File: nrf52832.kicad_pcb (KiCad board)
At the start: 2 copper layers, 66 parts, among them SW1 SW_Push, U1 nRF52832-QFxx, U2 AMS1117-3.3, U3 SX1308, U4 TP4056, U5 MC34063AD, U6 HT7127-1-SOT89, U7 TagConnect, Y1 32MHz

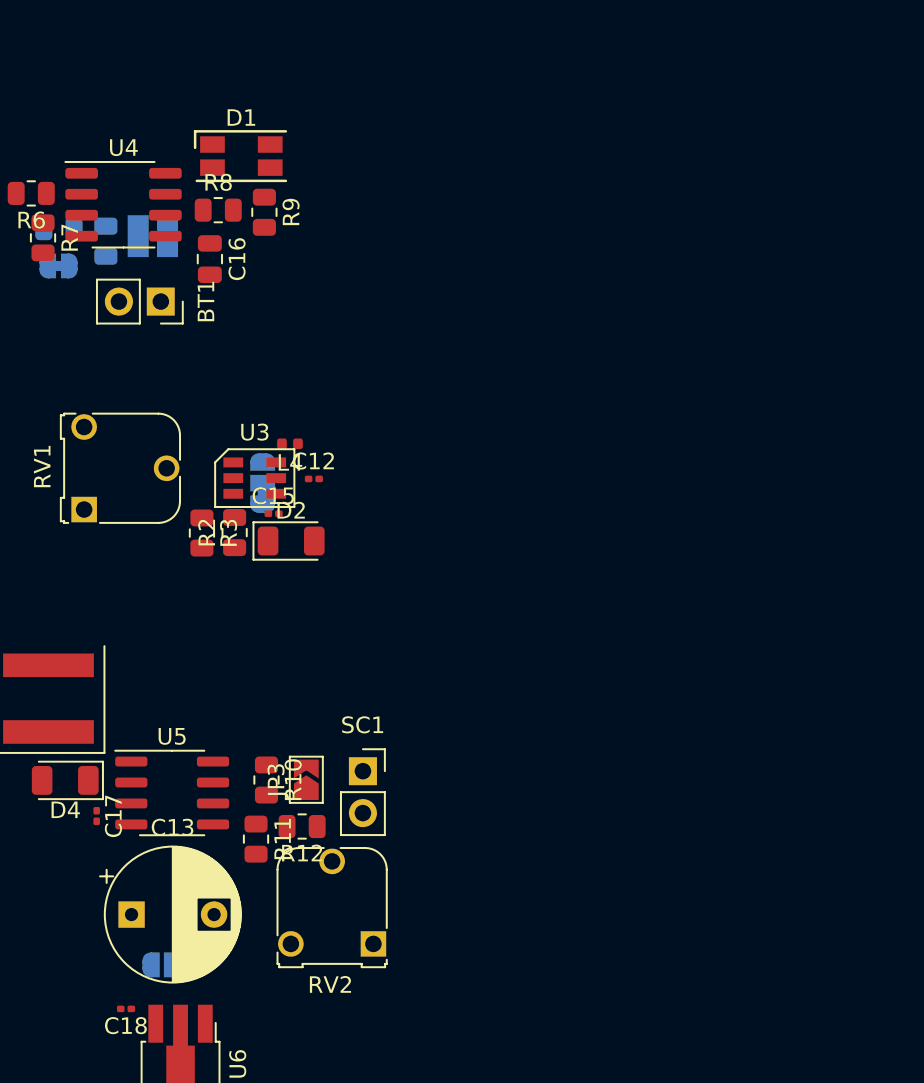
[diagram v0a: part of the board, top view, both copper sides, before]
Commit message: added AC power
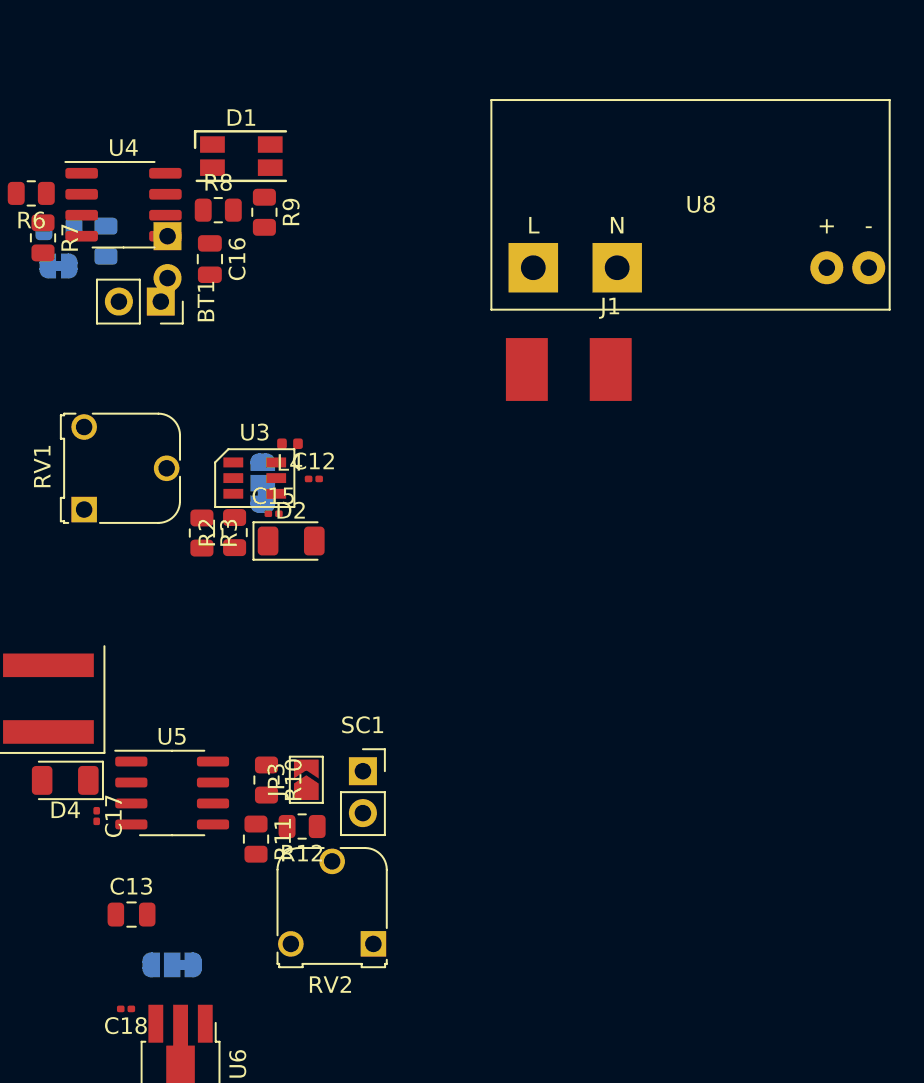
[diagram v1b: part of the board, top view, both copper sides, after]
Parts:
- added J1: Conn_01x02, smdpad:smdpad_01x02_2.54_3.81_2.54, F.Cu at (187.9, 56.0)
- added U8: WX-DC12003, aliexpress:WX-DC12003_vertical, F.Cu at (190.8, 44.8)
- C13: footprint Capacitor_THT:CP_Radial_D8.0mm_P5.00mm -> Capacitor_SMD:C_0805_2012Metric
- TH1: footprint smdpad:smdpad_01x02_1.27_2.54_0.51 -> Connector_PinSocket_2.54mm:PinSocket_1x02_P2.54mm_Vertical
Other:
- net class AC added: clearance 0.5, trace_width 1, via_dia 0.8, via_drill 0.5

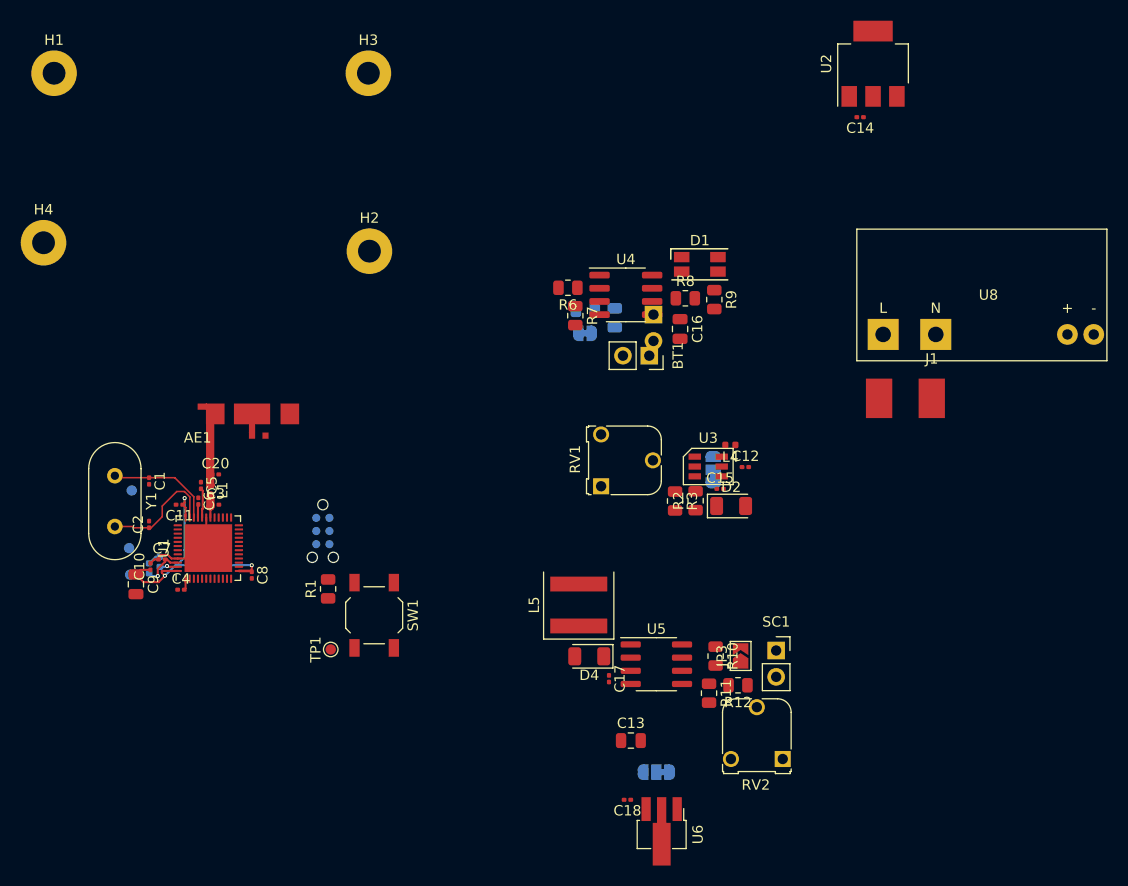
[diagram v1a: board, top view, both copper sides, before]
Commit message: optimized silkscreen
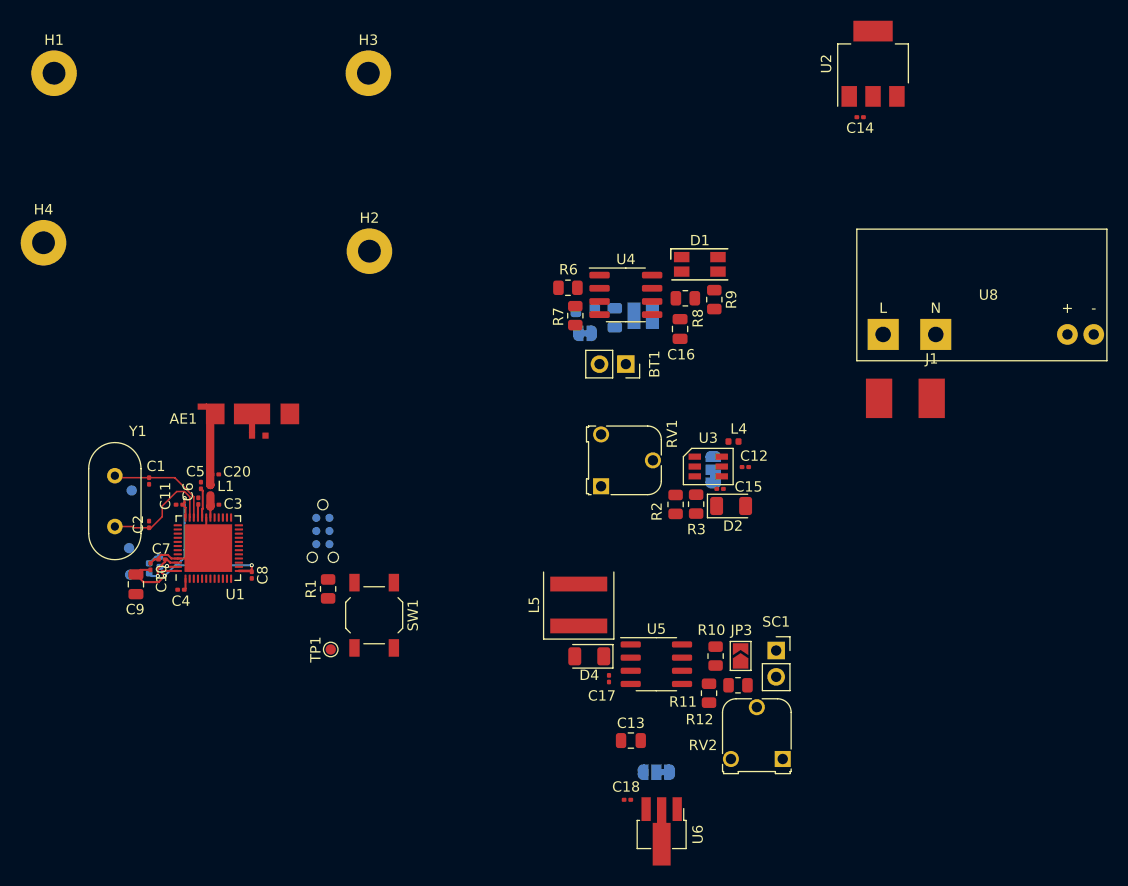
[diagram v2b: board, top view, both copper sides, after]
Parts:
- TH1: footprint Connector_PinSocket_2.54mm:PinSocket_1x02_P2.54mm_Vertical -> smdpad:smdpad_01x02_1.27_2.54_0.51
- moved BT1 2.40 mm to (158.4, 52.7)
- moved L4 0.45 mm to (168.8, 60.2)
- moved R3 0.33 mm to (163.2, 66.3)
- moved R2 0.33 mm to (165.2, 66.2)
- moved TH1 0.14 mm to (161.0, 48.1)
